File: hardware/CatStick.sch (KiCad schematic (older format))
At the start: 72 parts, among them J2 Antenna, J4 Conn_02x05_Odd_Even, J5 Conn_01x04, P1 USB_C_Plug_USB2.0, Q1 DMN6140L, SW1 SW_Push, SW2 RST, U1 CC1352R1F3RGZR, U2 AP2112K-3.3, U3 RFSW8006QTR7, U4 0900FM15D0039, U5 0900PC15A0036, U6 PE4259 RF Switch, U7 ATSAMD21E18A-A, U8 SX1262IMLTRT, Y1 32.768kHz, Y2 48MHz, Y3 32Mhz_10pF_10ppm

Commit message: completeComponents&footprints
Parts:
- BT1: value Battery -> a
- U4: footprint (none) -> CatSniffer:0900FM15D0039E
- U5: footprint (none) -> CatSniffer:0900FM15D0039E; Mouser# (none) -> 609-0900PC15A0036E; manf# (none) -> 0900PC15A0036E; provedor (none) -> Mouser
- U6: footprint Package_TO_SOT_SMD:SOT-363_SC-70-6 -> Package_TO_SOT_SMD:SOT-363_SC-70-6_Handsoldering
- U7: Mouser# (none) -> 556-ATSAMD21E18A-AU; manf# (none) -> ATSAMD21E18A-AU; provedor (none) -> Mouser
- U8: Mouser# (none) -> 947-SX1262IMLTRT; manf# (none) -> SX1262IMLTRT; provedor (none) -> Mouser
- Y1: footprint cc1350:FC-135 -> Crystal:Crystal_SMD_2012-2Pin_2.0x1.2mm_HandSoldering; LCSC# (none) -> C97603; manf# (none) -> SC-20S,32.768kHz,20PPM,9pF; provedor (none) -> LCSC
- Y2: footprint cc1350:TSX-3225 -> Crystal:Crystal_SMD_HC49-SD; LCSC# (none) -> C240990; manf# (none) -> 49MD-48.000-20-20-20/A; provedor (none) -> LCSC
- Y3: footprint (none) -> Crystal:Crystal_SMD_2520-4Pin_2.5x2.0mm; LCSC# (none) -> C255969; manf# (none) -> Q24FA20H0021700; provedor (none) -> LCSC
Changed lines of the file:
@@
 F 0 "Y1" H 1590 3895 50  0000 C CNN
 F 1 "32.768kHz" H 1590 3595 50  0000 C CNN
-F 2 "cc1350:FC-135" H 1590 3745 50  0001 C CNN
+F 2 "Crystal:Crystal_SMD_2012-2Pin_2.0x1.2mm_HandSoldering" H 1590 3745 50  0001 C CNN
 F 3 "" H 1590 3745 50  0000 C CNN
+F 4 "C97603" H 1590 3745 50  0001 C CNN "LCSC#"
+F 5 "SC-20S,32.768kHz,20PPM,9pF" H 1590 3745 50  0001 C CNN "manf#"
+F 6 "LCSC" H 1590 3745 50  0001 C CNN "provedor"
 	1    1590 3745
 	0    1    1    0
@@
 P 745 8995
 F 0 "BT1" H 845 9095 50  0000 L CNN
-F 1 "Battery" H 845 8995 50  0000 L CNN
+F 1 "a" H 845 8995 50  0000 L CNN
 F 2 "Connector_Molex:Molex_KK-254_AE-6410-02A_1x02_P2.54mm_Vertical" V 745 9055 50  0001 C CNN
 F 3 "" V 745 9055 50  0000 C CNN
@@
 F 0 "Y2" H 2745 1815 50  0000 L CNN
 F 1 "48MHz" H 2740 1750 50  0000 L CNN
-F 2 "cc1350:TSX-3225" H 2790 1490 50  0001 C CNN
+F 2 "Crystal:Crystal_SMD_HC49-SD" H 2790 1490 50  0001 C CNN
 F 3 "~" H 2790 1490 50  0001 C CNN
+F 4 "C240990" H 2790 1490 50  0001 C CNN "LCSC#"
+F 5 "49MD-48.000-20-20-20/A" H 2790 1490 50  0001 C CNN "manf#"
+F 6 "LCSC" H 2790 1490 50  0001 C CNN "provedor"
 	1    2790 1490
 	1    0    0    -1
@@
 F 0 "U5" H 7945 9360 50  0000 C CNN
 F 1 "0900PC15A0036" H 7945 9269 50  0000 C CNN
-F 2 "" H 7295 9045 50  0001 C CNN
+F 2 "CatSniffer:0900FM15D0039E" H 7295 9045 50  0001 C CNN
 F 3 "" H 7295 9045 50  0001 C CNN
+F 4 "609-0900PC15A0036E " H 8045 9045 50  0001 C CNN "Mouser#"
+F 5 "0900PC15A0036E" H 8045 9045 50  0001 C CNN "manf#"
+F 6 "Mouser" H 8045 9045 50  0001 C CNN "provedor"
 	1    8045 9045
 	1    0    0    -1
@@
 F 0 "U4" H 6935 3940 50  0000 C CNN
 F 1 "0900FM15D0039" H 6935 3849 50  0000 C CNN
-F 2 "" H 6285 3625 50  0001 C CNN
+F 2 "CatSniffer:0900FM15D0039E" H 6285 3625 50  0001 C CNN
 F 3 "" H 6285 3625 50  0001 C CNN
 F 4 "609-0900FM15D0039E" H 7035 3625 50  0001 C CNN "Mouser#"
@@
 F 2 "Package_QFP:TQFP-32_7x7mm_P0.8mm" H 18305 2175 50  0001 C CNN
 F 3 "http://ww1.microchip.com/downloads/en/DeviceDoc/SAM_D21_DA1_Family_Data%20Sheet_DS40001882E.pdf" H 17405 4025 50  0001 C CNN
+F 4 "556-ATSAMD21E18A-AU " H 17405 4025 50  0001 C CNN "Mouser#"
+F 5 "ATSAMD21E18A-AU " H 17405 4025 50  0001 C CNN "manf#"
+F 6 "Mouser" H 17405 4025 50  0001 C CNN "provedor"
 	1    17405 4025
 	1    0    0    -1
@@
 F 5 "IPC-7351B" H 14665 9085 50  0001 L BNN "STANDARD"
 F 6 "Semtech" H 14665 9085 50  0001 L BNN "MANUFACTURER"
+F 7 "947-SX1262IMLTRT " H 14665 9085 50  0001 C CNN "Mouser#"
+F 8 "SX1262IMLTRT " H 14665 9085 50  0001 C CNN "manf#"
+F 9 "Mouser" H 14665 9085 50  0001 C CNN "provedor"
 	1    14665 9085
 	1    0    0    -1
@@
 F 0 "Y3" H 13209 10021 50  0000 L CNN
 F 1 "32Mhz_10pF_10ppm" H 12040 9950 50  0000 L CNN
-F 2 "" H 13015 9975 50  0001 C CNN
+F 2 "Crystal:Crystal_SMD_2520-4Pin_2.5x2.0mm" H 13015 9975 50  0001 C CNN
 F 3 "~" H 13015 9975 50  0001 C CNN
+F 4 "C255969" H 13015 9975 50  0001 C CNN "LCSC#"
+F 5 "Q24FA20H0021700" H 13015 9975 50  0001 C CNN "manf#"
+F 6 "LCSC" H 13015 9975 50  0001 C CNN "provedor"
 	1    13015 9975
 	1    0    0    -1
@@
 F 0 "U6" H 20360 9815 50  0000 C CNN
 F 1 "PE4259 RF Switch" H 20360 9724 50  0000 C CNN
-F 2 "Package_TO_SOT_SMD:SOT-363_SC-70-6" H 20360 9490 50  0001 C CNN
+F 2 "Package_TO_SOT_SMD:SOT-363_SC-70-6_Handsoldering" H 20360 9490 50  0001 C CNN
 F 3 "http://cdn.macom.com/datasheets/maswss0115.pdf" H 20360 9490 50  0001 C CNN
 	1    20360 9390

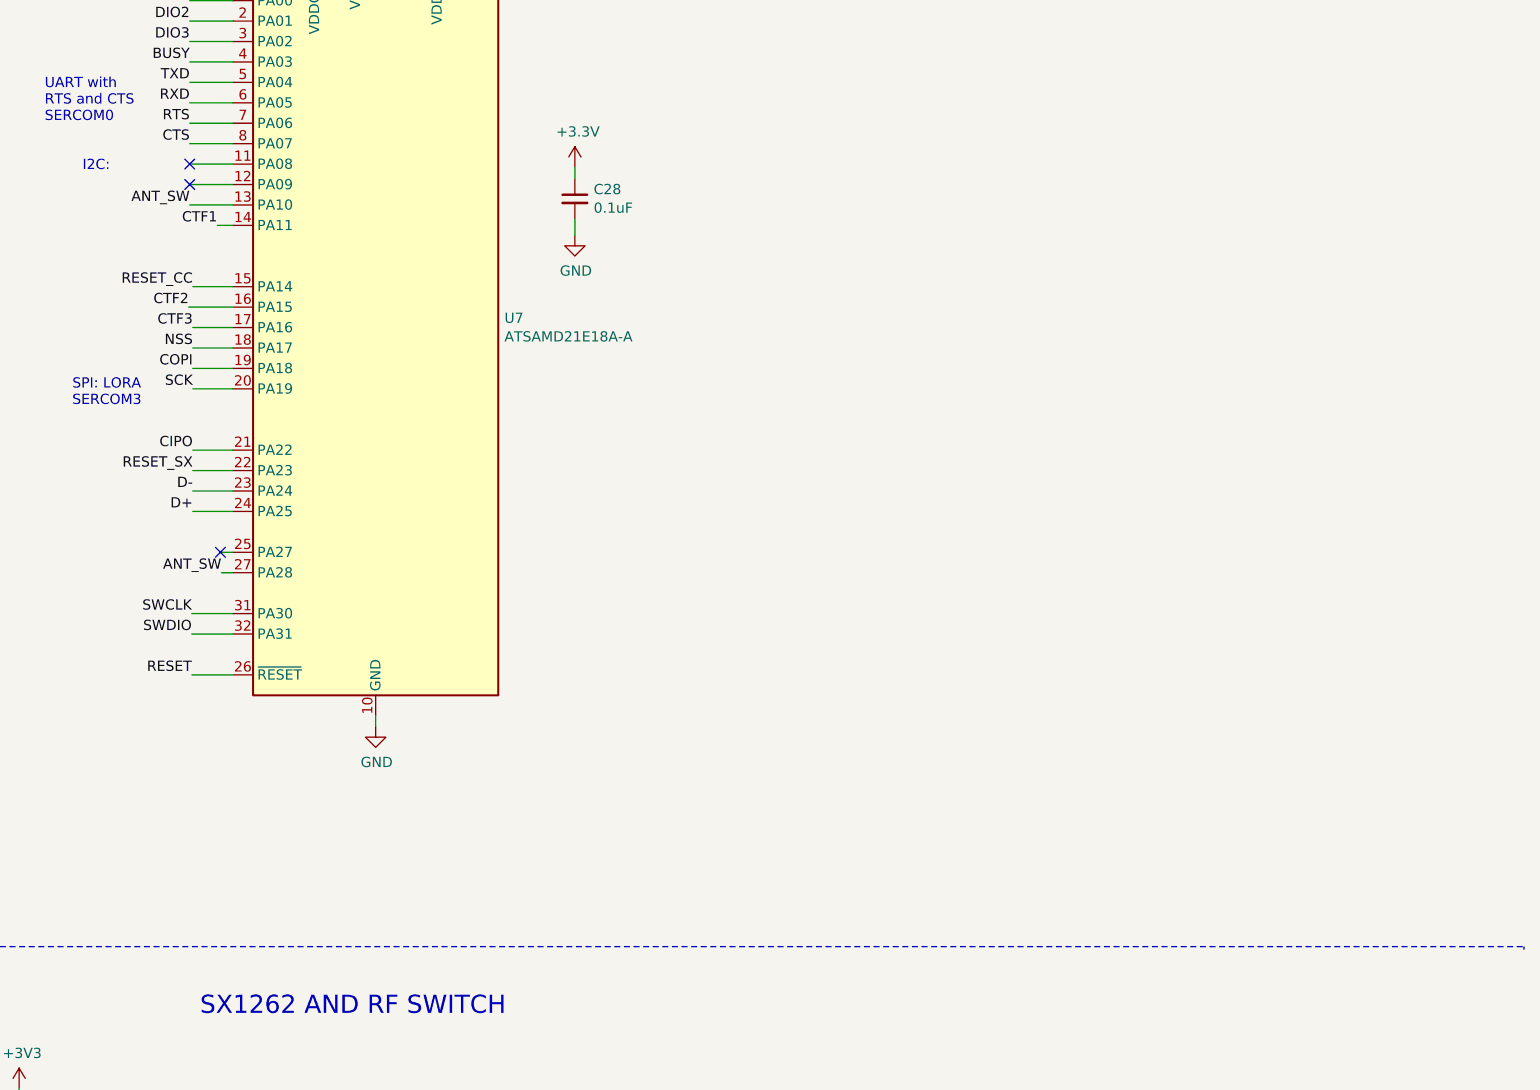
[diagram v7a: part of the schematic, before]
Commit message: addLEDSAMD21
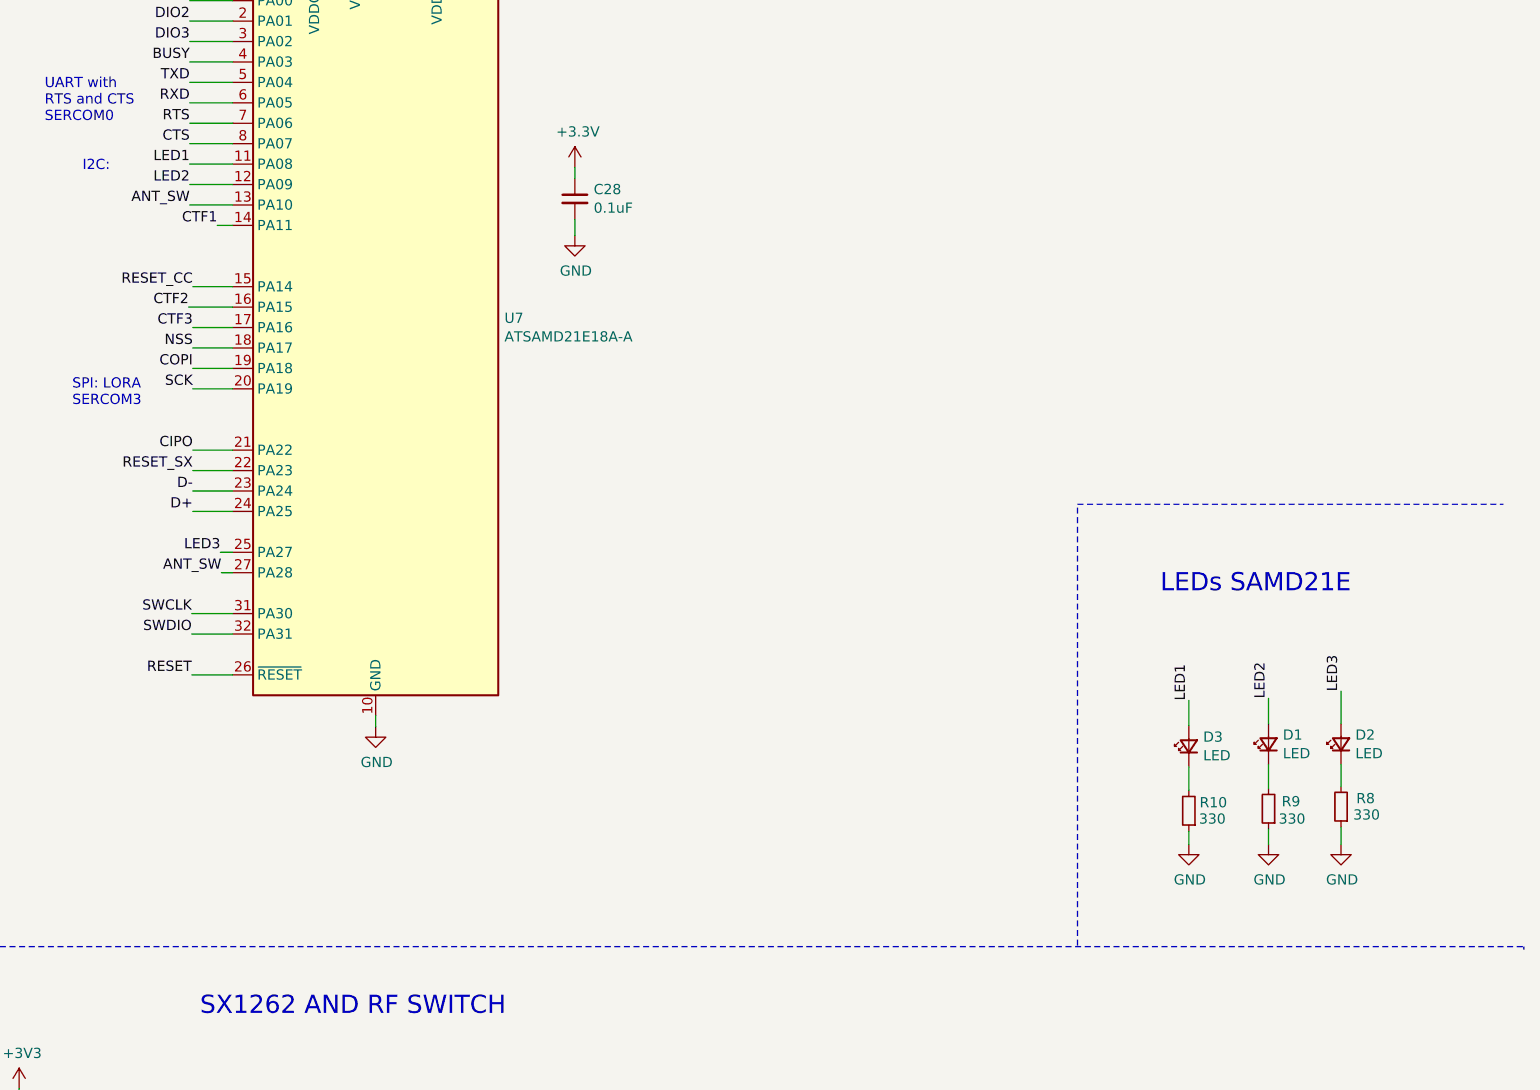
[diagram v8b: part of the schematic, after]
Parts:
- added D1, D2, D3: LED, LED_SMD:LED_0603_1608Metric_Pad1.05x0.95mm_HandSolder, symbol Device:LED_Small
- added R10, R8, R9: 330, Resistor_SMD:R_0603_1608Metric_Pad0.98x0.95mm_HandSolder, symbol Device:R_Small
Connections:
- net GND: now also R10.1, R8.1, R9.1
- net LED1: now reaches U7.11 (PA08)
- net LED1: now also D3.2 (A)
- net LED2: now reaches U7.12 (PA09)
- net LED2: now also D1.2 (A)
- net LED3: now reaches U7.25 (PA27)
- net LED3: now also D2.2 (A)
- new net: D3.1 (K), R10.2
- new net: D1.1 (K), R9.2
- new net: D2.1 (K), R8.2
- no-connect marks 27 -> 24
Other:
- note added: "LEDs SAMD21E\n\n"
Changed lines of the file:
@@
 Wire Wire Line
 	16510 4025 16705 4025
-NoConn ~ 16495 3225
-NoConn ~ 16495 3325
-NoConn ~ 16645 5125
 $Comp
 L power:GND #PWR067
@@
 Wire Notes Line
 	5025 11850 5035 11850
+$Comp
+L Device:LED_Small D3
+U 1 1 6087770B
+P 21385 6075
+F 0 "D3" V 21431 6005 50  0000 R CNN
+F 1 "LED" V 21340 6005 50  0000 R CNN
+F 2 "LED_SMD:LED_0603_1608Metric_Pad1.05x0.95mm_HandSolder" V 21385 6075 50  0001 C CNN
+F 3 "~" V 21385 6075 50  0001 C CNN
+F 4 " C524045" H 21385 6075 50  0001 C CNN "LCSC#"
+F 5 "DY-0603HBC-L-SMG" H 21385 6075 50  0001 C CNN "manf#"
+F 6 "LCSC" H 21385 6075 50  0001 C CNN "provedor"
+	1    21385 6075
+	0    -1   -1   0
+$EndComp
+$Comp
+L Device:R_Small R10
+U 1 1 60877B07
+P 21385 6390
+F 0 "R10" H 21265 6350 50  0000 C CNN
+F 1 "330" H 21270 6430 50  0000 C CNN
+F 2 "Resistor_SMD:R_0603_1608Metric_Pad0.98x0.95mm_HandSolder" H 21385 6390 50  0001 C CNN
+F 3 "~" H 21385 6390 50  0001 C CNN
+F 4 "C325681" H 21385 6390 50  0001 C CNN "LCSC#"
+F 5 "RMC0603301%N" H 21385 6390 50  0001 C CNN "manf#"
+F 6 "LCSC" H 21385 6390 50  0001 C CNN "provedor"
+	1    21385 6390
+	-1   0    0    1
+$EndComp
+$Comp
+L power:GND #PWR068
+U 1 1 6089575C
+P 21385 6555
+F 0 "#PWR068" H 21385 6305 50  0001 C CNN
+F 1 "GND" H 21390 6382 50  0000 C CNN
+F 2 "" H 21385 6555 50  0001 C CNN
+F 3 "" H 21385 6555 50  0001 C CNN
+	1    21385 6555
+	1    0    0    -1
+$EndComp
+Wire Wire Line
+	21385 6555 21385 6490
+Wire Wire Line
+	21385 6290 21385 6175
+Text Label 21385 5850 1    50   ~ 0
+LED1
+Wire Wire Line
+	21385 5850 21385 5975
+$Comp
+L Device:LED_Small D1
+U 1 1 6092AB5A
+P 21775 6065
+F 0 "D1" V 21821 5995 50  0000 R CNN
+F 1 "LED" V 21730 5995 50  0000 R CNN
+F 2 "LED_SMD:LED_0603_1608Metric_Pad1.05x0.95mm_HandSolder" V 21775 6065 50  0001 C CNN
+F 3 "~" V 21775 6065 50  0001 C CNN
+F 4 " C524045" H 21775 6065 50  0001 C CNN "LCSC#"
+F 5 "DY-0603HBC-L-SMG" H 21775 6065 50  0001 C CNN "manf#"
+F 6 "LCSC" H 21775 6065 50  0001 C CNN "provedor"
+	1    21775 6065
+	0    -1   -1   0
+$EndComp
+$Comp
+L Device:R_Small R9
+U 1 1 6092AF39
+P 21775 6380
+F 0 "R9" H 21665 6345 50  0000 C CNN
+F 1 "330" H 21660 6430 50  0000 C CNN
+F 2 "Resistor_SMD:R_0603_1608Metric_Pad0.98x0.95mm_HandSolder" H 21775 6380 50  0001 C CNN
+F 3 "~" H 21775 6380 50  0001 C CNN
+F 4 "C325681" H 21775 6380 50  0001 C CNN "LCSC#"
+F 5 "RMC0603301%N" H 21775 6380 50  0001 C CNN "manf#"
+F 6 "LCSC" H 21775 6380 50  0001 C CNN "provedor"
+	1    21775 6380
+	-1   0    0    1
+$EndComp
+$Comp
+L power:GND #PWR069
+U 1 1 6092B333
+P 21775 6555
+F 0 "#PWR069" H 21775 6305 50  0001 C CNN
+F 1 "GND" H 21780 6382 50  0000 C CNN
+F 2 "" H 21775 6555 50  0001 C CNN
+F 3 "" H 21775 6555 50  0001 C CNN
+	1    21775 6555
+	1    0    0    -1
+$EndComp
+Text Label 21775 5840 1    50   ~ 0
+LED2
+Text Label 22130 5805 1    50   ~ 0
+LED3
+$Comp
+L Device:LED_Small D2
+U 1 1 6092B5D1
+P 22130 6065
+F 0 "D2" V 22176 5995 50  0000 R CNN
+F 1 "LED" V 22085 5995 50  0000 R CNN
+F 2 "LED_SMD:LED_0603_1608Metric_Pad1.05x0.95mm_HandSolder" V 22130 6065 50  0001 C CNN
+F 3 "~" V 22130 6065 50  0001 C CNN
+F 4 " C524045" H 22130 6065 50  0001 C CNN "LCSC#"
+F 5 "DY-0603HBC-L-SMG" H 22130 6065 50  0001 C CNN "manf#"
+F 6 "LCSC" H 22130 6065 50  0001 C CNN "provedor"
+	1    22130 6065
+	0    -1   -1   0
+$EndComp
+$Comp
+L Device:R_Small R8
+U 1 1 6092BA07
+P 22130 6370
+F 0 "R8" H 22010 6330 50  0000 C CNN
+F 1 "330" H 22005 6410 50  0000 C CNN
+F 2 "Resistor_SMD:R_0603_1608Metric_Pad0.98x0.95mm_HandSolder" H 22130 6370 50  0001 C CNN
+F 3 "~" H 22130 6370 50  0001 C CNN
+F 4 "C325681" H 22130 6370 50  0001 C CNN "LCSC#"
+F 5 "RMC0603301%N" H 22130 6370 50  0001 C CNN "manf#"
+F 6 "LCSC" H 22130 6370 50  0001 C CNN "provedor"
+	1    22130 6370
+	-1   0    0    1
+$EndComp
+$Comp
+L power:GND #PWR070
+U 1 1 6092BD69
+P 22130 6555
+F 0 "#PWR070" H 22130 6305 50  0001 C CNN
+F 1 "GND" H 22135 6382 50  0000 C CNN
+F 2 "" H 22130 6555 50  0001 C CNN
+F 3 "" H 22130 6555 50  0001 C CNN
+	1    22130 6555
+	1    0    0    -1
+$EndComp
+Wire Wire Line
+	21775 5965 21775 5840
+Wire Wire Line
+	21775 6280 21775 6165
+Wire Wire Line
+	21775 6555 21775 6480
+Wire Wire Line
+	22130 5805 22130 5965
+Wire Wire Line
+	22130 6165 22130 6270
+Wire Wire Line
+	22130 6555 22130 6470
+Text Label 16495 3225 2    50   ~ 0
+LED1
+Text Label 16495 3325 2    50   ~ 0
+LED2
+Text Label 16645 5125 2    50   ~ 0
+LED3
+Text Notes 21245 5475 0    89   ~ 0
+LEDs SAMD21E\n\n
+Wire Notes Line
+	20840 7050 20840 4890
+Wire Notes Line
+	20840 4890 22925 4890
 $EndSCHEMATC
